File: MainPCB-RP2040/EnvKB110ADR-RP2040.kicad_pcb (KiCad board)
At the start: 2 copper layers, 429.5 x 125 mm, 267 parts, among them J2 EVQPU, J5 Conn_01x03_Male, U1 TLV75533PDBVR, U3 RP2040, Y1 3225_4P

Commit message: general corrections and tweaks
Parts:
- D3, R8: moved to F.Cu
- moved R8 29.5 mm to (388.4, 62.9), turned to 270 degrees
- moved D3 28.3 mm to (387.1, 62.9), turned to 90 degrees
- moved R12 2.21 mm to (388.6, 55.6), turned to 90 degrees
- moved C3 0.50 mm to (423.6, 61.4)
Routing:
- net /GPIO25: track 5.10 -> 35.4 mm, vias 0 -> 3
- net VBUS: track 18.2 -> 17.2 mm
- net /SWCLK: track 36.2 -> 35.7 mm
- net row1: vias 1 -> 0
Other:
- net class Default: clearance 0.2 -> 0.127
- rule trace_clearance: 0.2 -> 0.127
- board text added: "GP25"
- board text added: "PWR"

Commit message: replaced switch footprints with stronger versions and SMT assembly compatible versions
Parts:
- added stab1: MountingHole, Mounting_Keyboard_Stabilizer:Stabilizer_Cherry_MX_2u, F.Cu at (304.3, 89.7)
- added stab2: MountingHole, Mounting_Keyboard_Stabilizer:Stabilizer_Cherry_MX_2u, F.Cu at (301.9, 127.7)
- added stab3: MountingHole, Mounting_Keyboard_Stabilizer:Stabilizer_Cherry_MX_2u, F.Cu at (59.0, 146.8)
- added stab4: MountingHole, Mounting_Keyboard_Stabilizer:Stabilizer_Cherry_MX_2u, F.Cu at (297.2, 146.8)
- added stab5: MountingHole, Mounting_Keyboard_Stabilizer:Stabilizer_Cherry_MX_6.25u, F.Cu at (168.6, 165.8)
- added stab6: MountingHole, Mounting_Keyboard_Stabilizer:Stabilizer_Cherry_MX_2u, F.Cu at (311.4, 118.2)
- K_100, K_101, K_102, K_112, K_113, K_114, K_116, K_12, K_13, K_14, K_15, K_16, K_17, K_18, K_19, K_20, K_21, K_22, K_23, K_24, K_25, K_26, K_27, K_28, K_29, K_30, K_31, K_32, K_33, K_34, K_35, K_36, K_37, K_38, K_39, K_40, K_42, K_43, K_44, K_45, K_46, K_47, K_48, K_50, K_51, K_52, K_53, K_54, K_55, K_56, K_57, K_58, K_59, K_60, K_61, K_63, K_64, K_65, K_66, K_67, K_68, K_71, K_72, K_73, K_74, K_75, K_76, K_77, K_78, K_79, K_80, K_81, K_82, K_83, K_84, K_85, K_87, K_88, K_89, K_90, K_91, K_92, K_93, K_94, K_95, K_96, K_97, K_99: footprint MX_Only:MXOnly-1U-Hotswap -> MX_Only:MXOnly-1U-Hotswap-custom
- K_103, K_115, K_41, K_62, K_69: footprint MX_Only:MXOnly-2U-Hotswap -> MX_Only:MXOnly-1U-Hotswap-custom
- K_104, K_105, K_106, K_108, K_109, K_110, K_111, K_86: footprint MX_Only:MXOnly-1.25U-Hotswap -> MX_Only:MXOnly-1U-Hotswap-custom
- K_107: footprint MX_Only:MXOnly-6.25U-Hotswap-ReversedStabilizers -> MX_Only:MXOnly-1U-Hotswap-custom
- K_49, K_ANSI_3: footprint MX_Only:MXOnly-1.5U-Hotswap -> MX_Only:MXOnly-1U-Hotswap-custom
- K_70: footprint MX_Only:MXOnly-1.75U-Hotswap -> MX_Only:MXOnly-1U-Hotswap-custom
- K_98: footprint MX_Only:MXOnly-2.75U-Hotswap -> MX_Only:MXOnly-1U-Hotswap-custom
- K_ANSI_1, K_ANSI_2: footprint MX_Only:MXOnly-2.25U-Hotswap -> MX_Only:MXOnly-1U-Hotswap-custom
- moved G*** 0.51 mm to (446.1, 68.1)
- turned K_ANSI_3 to 270 degrees
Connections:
- U3 pad 2: /GPIO0 -> (no net)
- USB1 pad 3: Net-(USB1-Pad3) -> (no net)
- USB1 pad 9: Net-(USB1-Pad9) -> (no net)
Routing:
- net col8: track 351.4 -> 366.1 mm
- net col14: track 271.4 -> 282.1 mm
- net col13: track 257.6 -> 265.3 mm
- net col12: track 251.6 -> 256.5 mm
- net Net-(D_ANSI_1-Pad2): track 11.3 -> 15.2 mm
- net col9: track 332.6 -> 335.2 mm
- net row4: track 460.0 -> 459.0 mm
- net +1V1: track 14.7 -> 15.6 mm

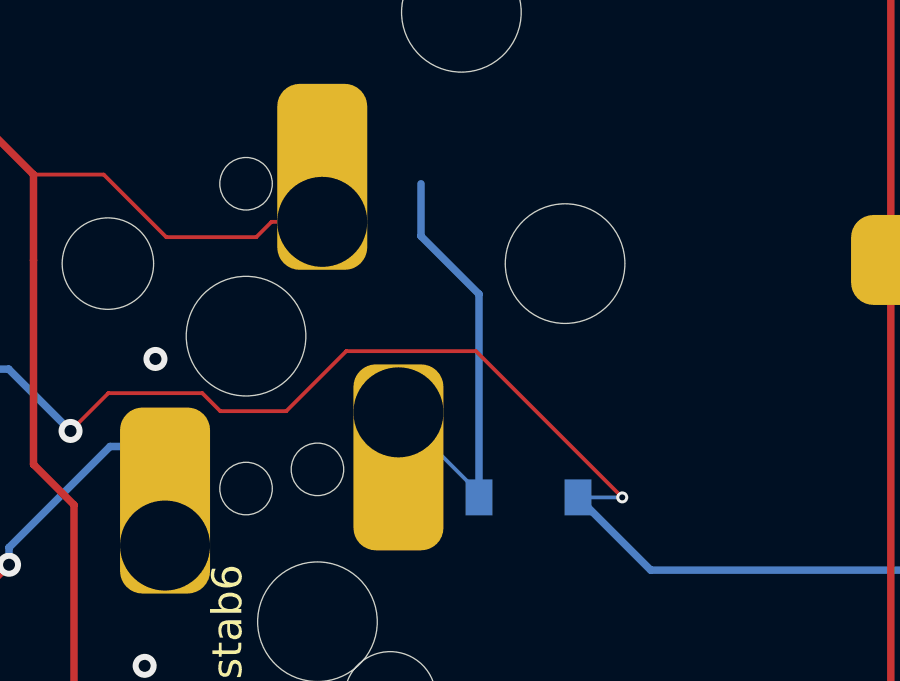
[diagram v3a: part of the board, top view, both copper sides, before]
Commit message: fixed a random trace that was left over from something else.
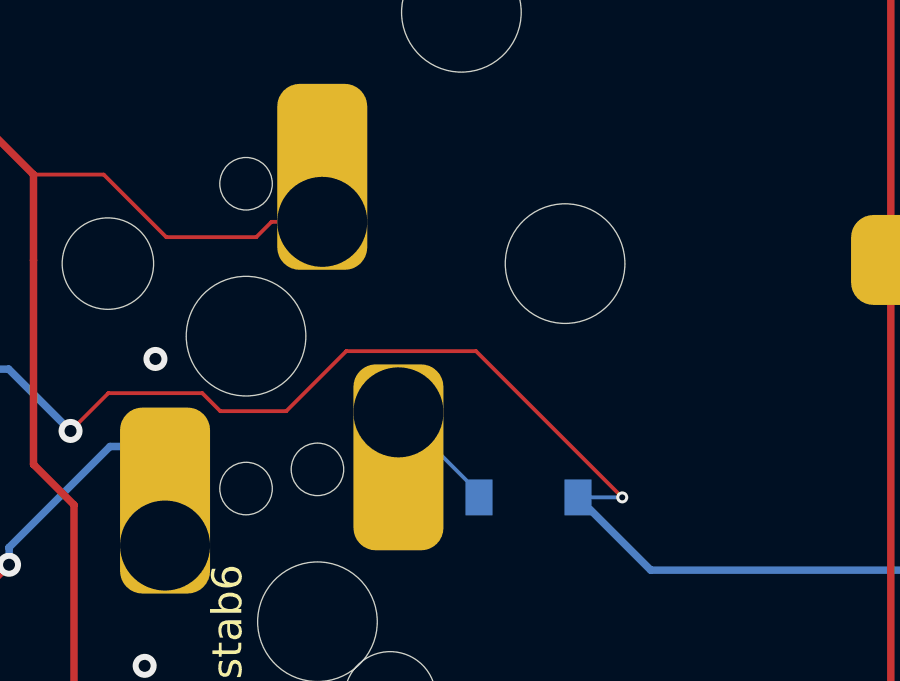
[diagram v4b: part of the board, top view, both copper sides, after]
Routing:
- net Net-(D_ANSI_1-Pad2): track 15.2 -> 3.95 mm
